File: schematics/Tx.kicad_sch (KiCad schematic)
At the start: 26 parts, among them J1 Conn_02x15_Counter_Clockwise, J2 SMP-MSLD-PCS17T, J3 PCB edge, U1 HMC431, U2 PAT1220-C-10DB, U3 TQP5527, U5 MCP1700T-3002E/MB

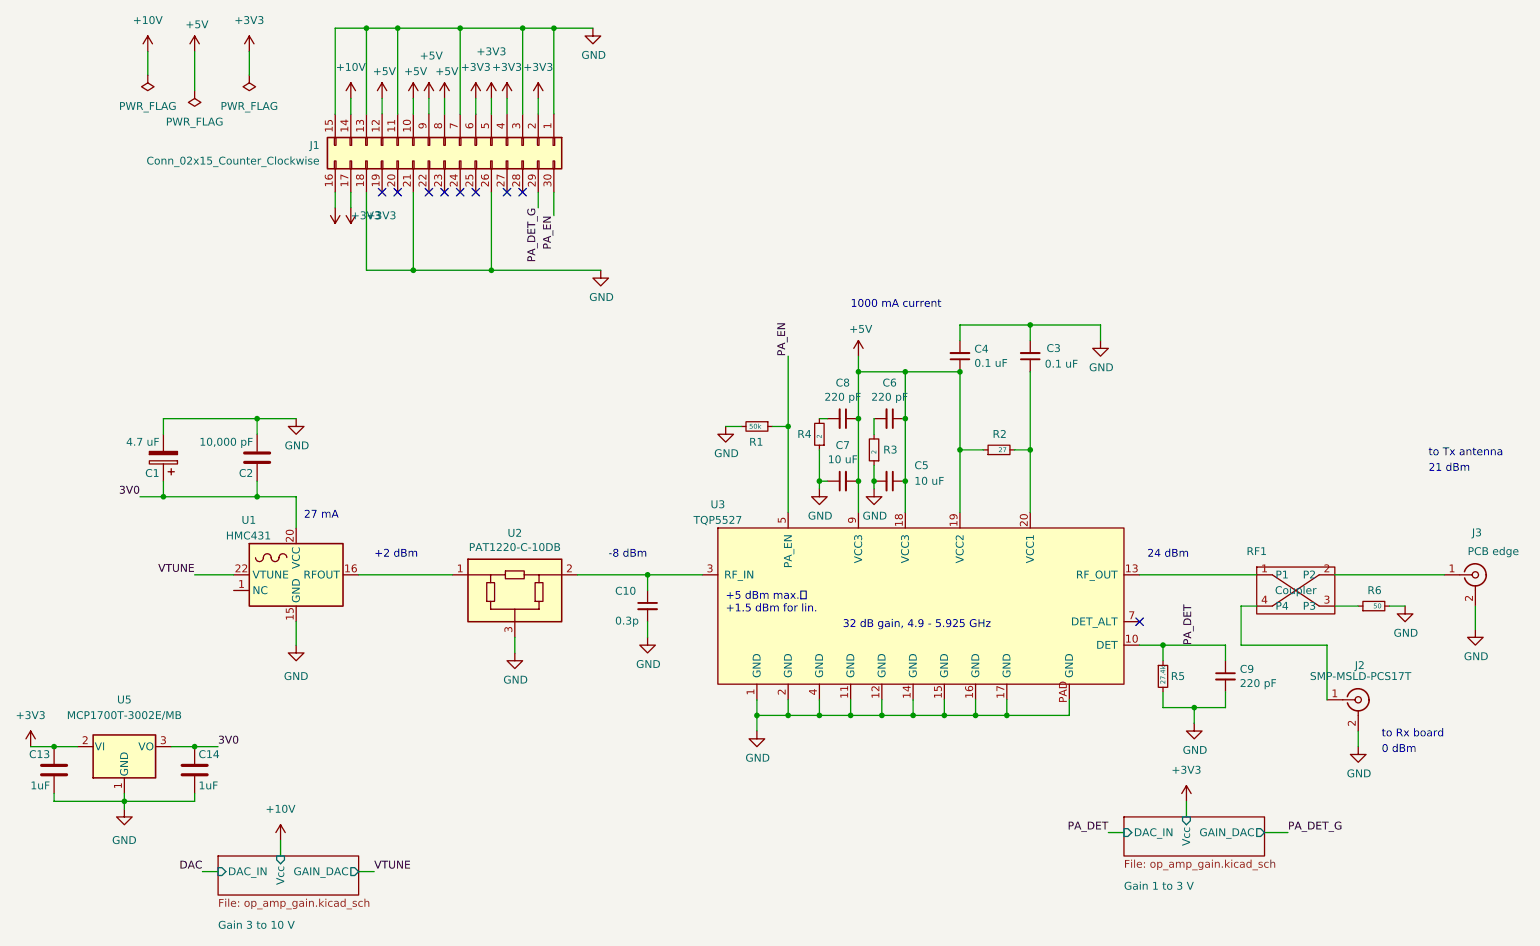
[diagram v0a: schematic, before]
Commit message: Added Rx board
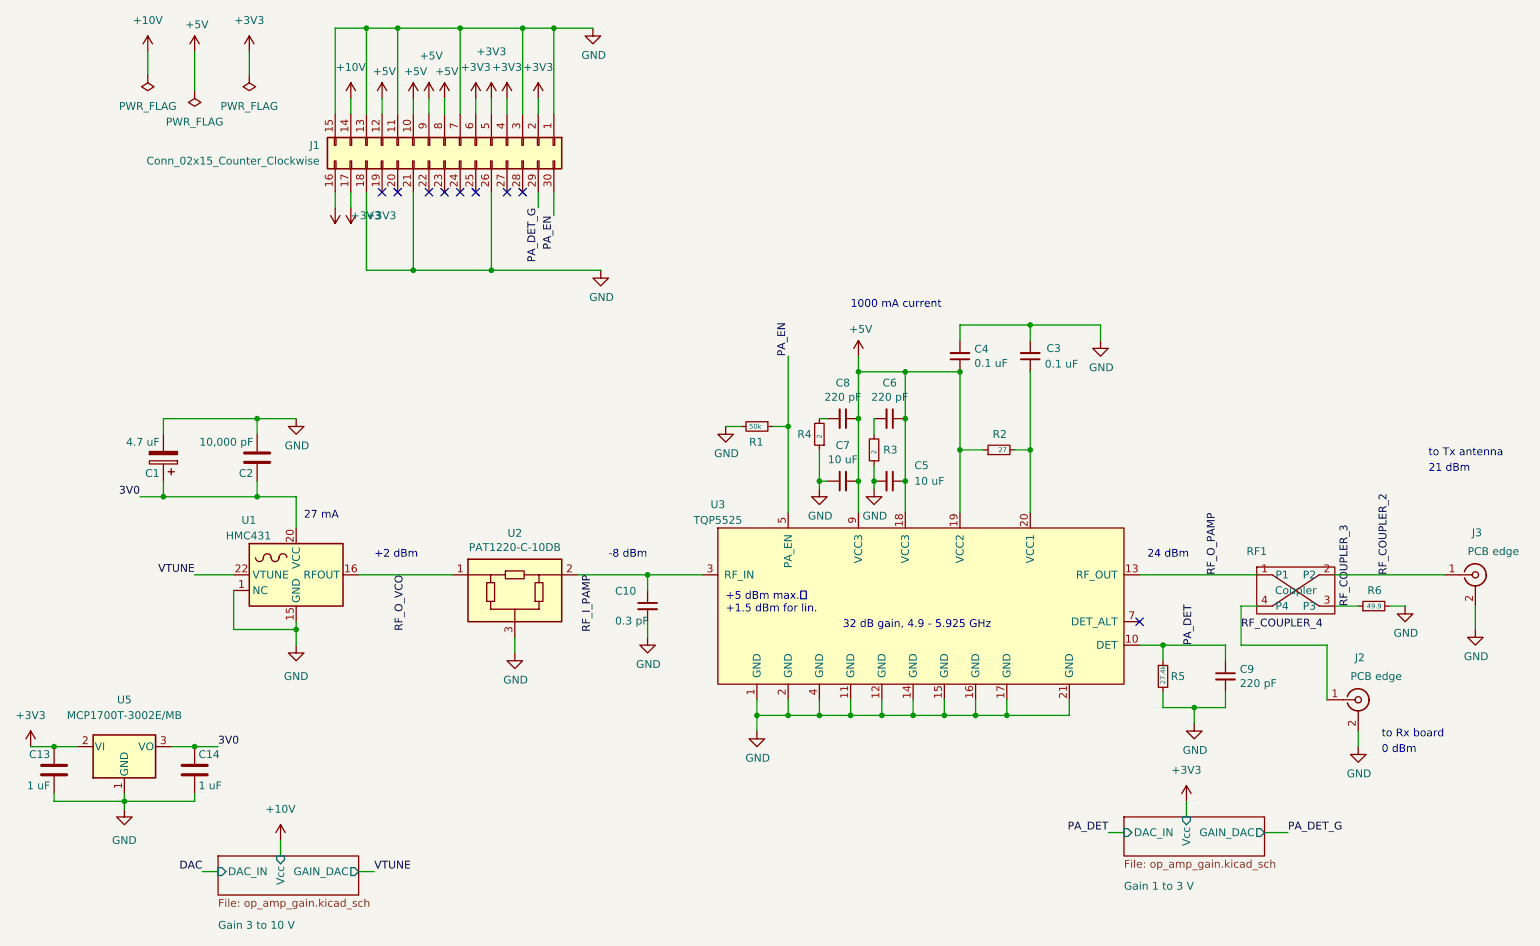
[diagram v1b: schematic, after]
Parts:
- C10: value 0.3p -> 0.3 pF; Candidate (none) -> 0402N0R3B500CT
- C13, C14: value 1uF -> 1 uF; Candidate ceramic -> CL10B105KA8NNNL
- C3, C4: Candidate RM LMK105 BJ104KV-F -> LMK105 BJ104KV-F
- C5, C7: Candidate C1608X5R1A106M but in 0402 pkg -> CL05A106MP5NUNC
- C6, C8, C9: Candidate RM UMK105BJ221KV-F -> UMK105BJ221KV-F
- J1: footprint (none) -> Connector_Molex:Molex_SlimStack_52991-0308_2x15_P0.50mm_Vertical
- J2: value SMP-MSLD-PCS17T -> PCB edge; footprint (none) -> Connector_Coaxial:SMA_Molex_73251-1153_EdgeMount_Horizontal; Candidate (none) -> 0732511150
- J3: footprint (none) -> Connector_Coaxial:SMA_Molex_73251-1153_EdgeMount_Horizontal
- R3, R4: footprint Resistor_SMD:R_0402_1005Metric -> Resistor_SMD:R_0603_1608Metric; Candidate RM UMK105BJ221KV-F -> ESR03EZPF2R00
- R5: footprint Resistor_SMD:R_0402_1005Metric -> Resistor_SMD:R_0603_1608Metric; Candidate ERJ-8ENF2742 but in 0402 pkg -> ERJ-PB3D2742V
- R6: value 50 -> 49.9; Candidate (none) -> ERJ-U02F49R9X
- RF1: footprint (none) -> RF_traces:-24 dB coupler 5.5 GHz OSHpark 4 layers
- U3: value TQP5527 -> TQP5525
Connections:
- net GND: now also U1.1 (NC), U1.10 (NC), U1.11 (NC), U1.12 (NC), U1.13 (NC), U1.14 (NC), U1.17 (NC), U1.18 (NC), U1.19 (NC), U1.2 (NC), U1.21 (NC), U1.23 (NC), U1.24 (NC), U1.3 (NC), U1.4 (NC), U1.5 (NC), U1.6 (NC), U1.7 (NC), U1.8 (NC), U1.9 (NC), U3.21 (GND); no longer U3.PAD (GND)
- net RF_O_VCO: now reaches U1.16 (RFOUT), U2.1
- net RF_I_PAMP: now reaches C10.1, U2.2, U3.3 (RF_IN)
- net RF_O_PAMP: now reaches RF1.1 (P1), U3.13 (RF_OUT)
- net RF_COUPLER_2: now reaches J3.1 (In), RF1.2 (P2)
- net RF_COUPLER_4: now reaches J2.1 (In), RF1.4 (P4)
- net RF_COUPLER_3: now reaches R6.1, RF1.3 (P3)
